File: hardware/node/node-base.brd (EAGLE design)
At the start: 100 x 80 mm, 19 parts, among them U1 INA322_DGK_8, U2 LMV551_DBV_5

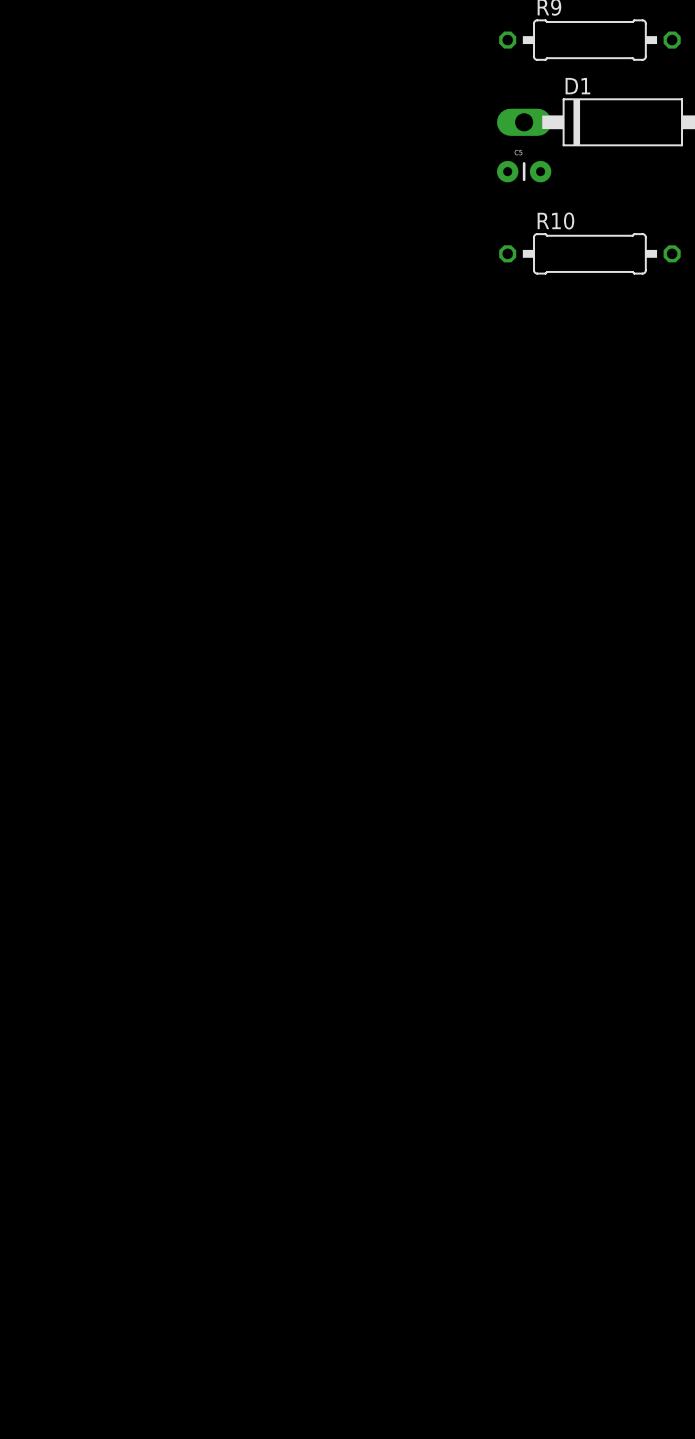
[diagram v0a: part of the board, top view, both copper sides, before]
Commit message: NODEHW: Added MCU power
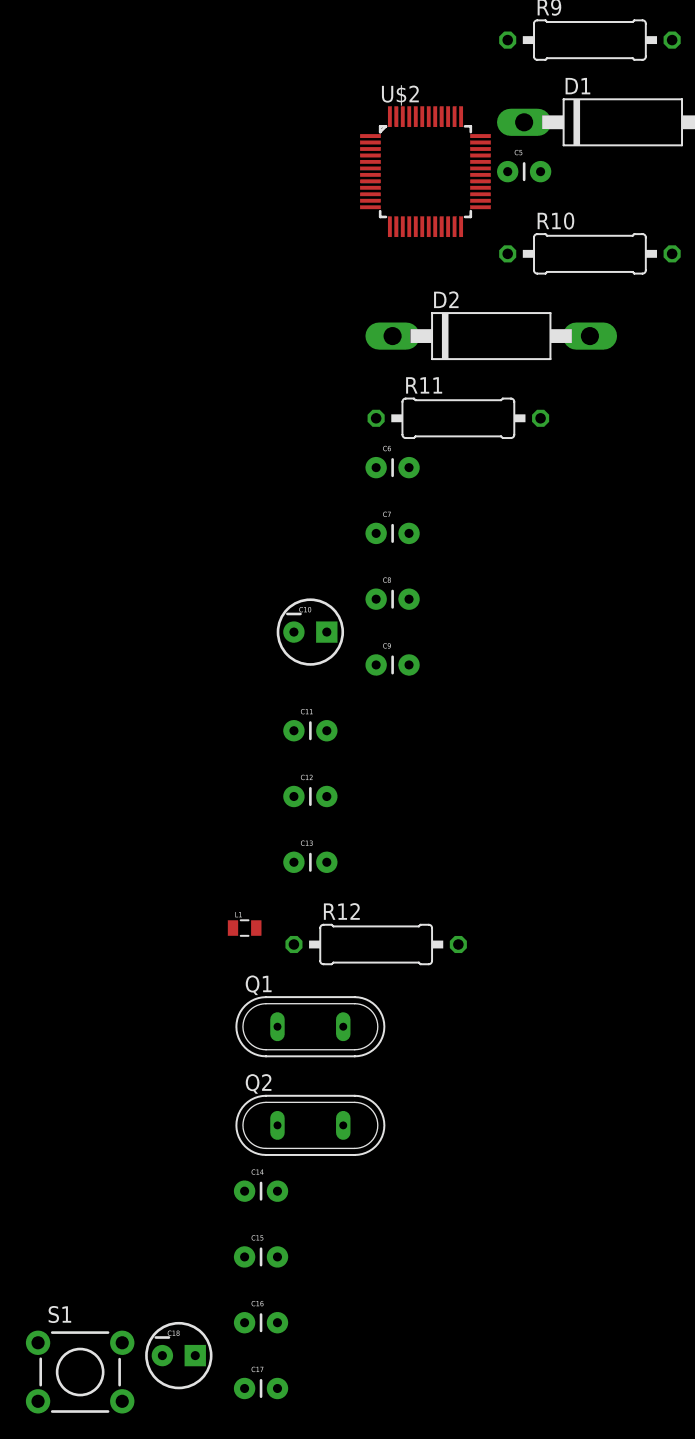
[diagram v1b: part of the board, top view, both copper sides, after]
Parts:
- added C10, C18: 10u, SparkFun-Capacitors:CPOL-RADIAL-10UF-25V
- added C11, C12, C13: 10n, SparkFun-Capacitors:CAP-PTH-SMALL
- added C14, C15, C16, C17: 7p5, SparkFun-Capacitors:CAP-PTH-SMALL
- added C6, C7, C8, C9: 100n, SparkFun-Capacitors:CAP-PTH-SMALL
- added D2: BAS81, diode:CB417-15
- added L1: (no value), SparkFun-Passives:0805
- added Q1, Q2: (no value), special:QS
- added R11: 10M, resistor:0309/12
- added R12: 1R, resistor:0309/12
- added S1: SPSTPTH_EZ, SparkFun-Electromechanical:TACTILE-PTH-EZ
- added U$2: EFM32ZG222EFM32ZG222F32, FullyCustom:QFP48
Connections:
- new net N$12: S1.3, U$2.16
- new net N$14: C14.1, Q1.1, U$2.12
- new net N$16: C15.1, Q1.2, U$2.11
- new net N$17: C16.1, Q2.1, U$2.21
- new net N$18: C17.1, Q2.2, U$2.20
- new net N$23: C18.1, U$2.29
- new net N$3: D2.A, R11.1, U$2.7
- new net N$6: L1.2, R12.1
- new net N$8: C11.1, C12.1, C13.1, R12.2, U$2.19, U$2.23
- net +3V3: now also C10.1, C6.1, C7.1, C8.1, C9.1, L1.1, U$2.22, U$2.28, U$2.4, U$2.43
- net DETECT_OUT: now also U$2.6
- net GND: now also C10.2, C11.2, C12.2, C13.2, C14.2, C15.2, C16.2, C17.2, C18.2, C6.2, C7.2, C8.2, C9.2, S1.1, U$2.18, U$2.44, U$2.5
- net N$2: now also R11.2
- net VCC/2: now also D2.C

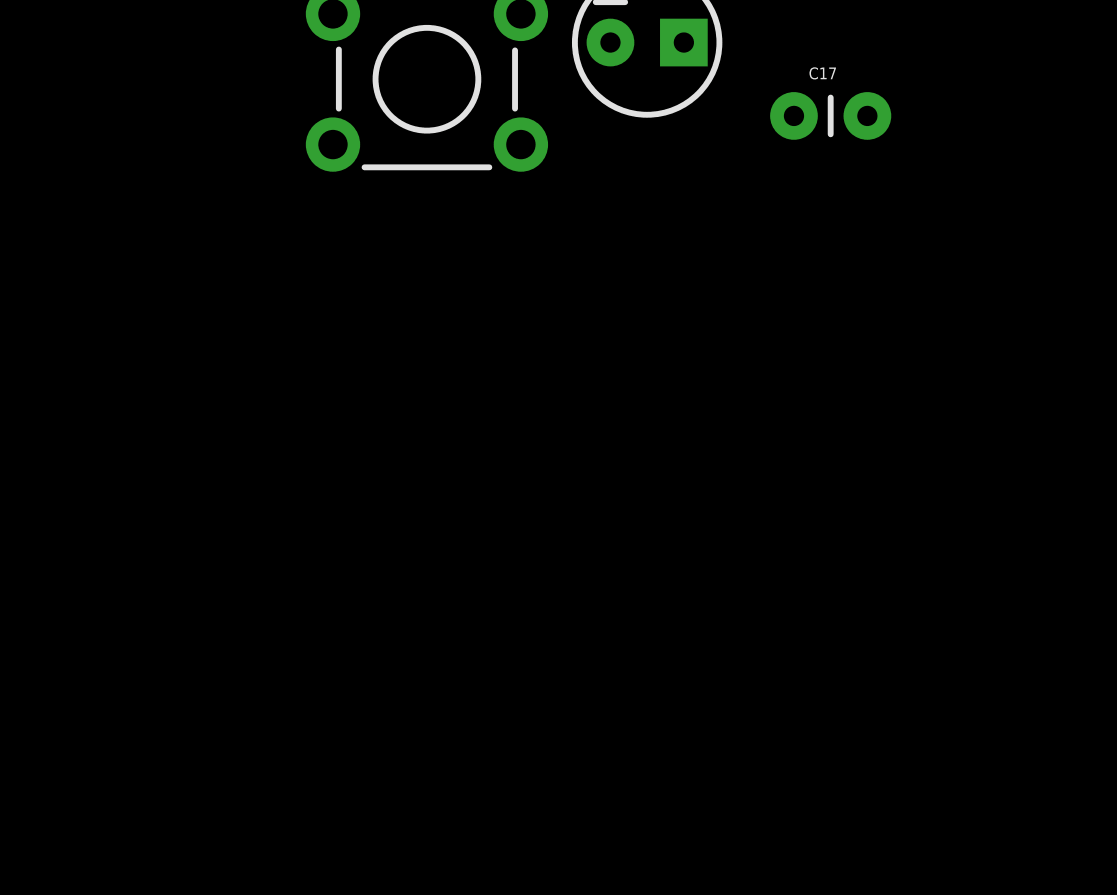
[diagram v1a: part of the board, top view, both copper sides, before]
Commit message: NODE: Added radio
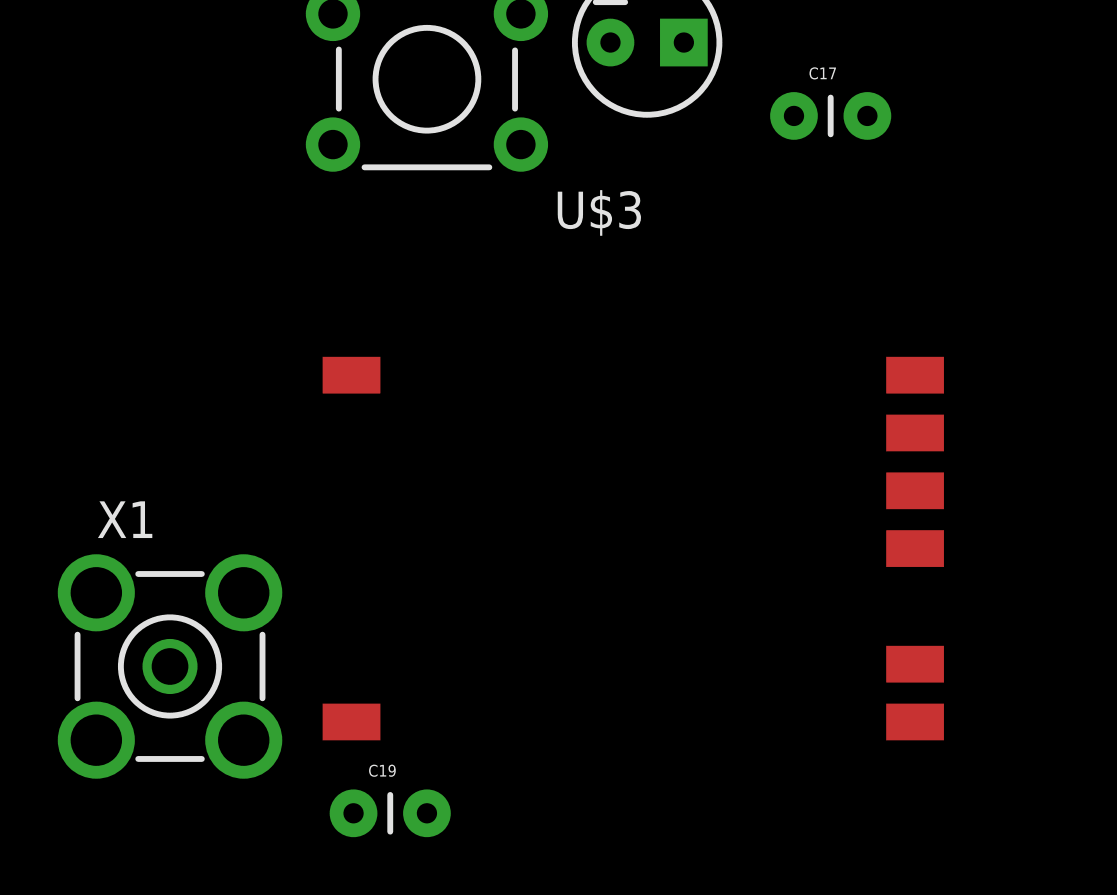
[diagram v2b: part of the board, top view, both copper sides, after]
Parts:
- added C19: 100n, SparkFun-Capacitors:CAP-PTH-SMALL
- added U$3: RFM69, Moteino:RFM69W-MINPADS
- added X1: BU-SMA-V, con-coax:BU-SMA-V
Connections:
- new net N$13: U$2.26, U$3.MISO
- new net N$15: U$2.27, U$3.MOSI
- new net N$19: U$2.35, U$3.NSS
- new net N$20: U$2.36, U$3.SCK
- new net N$22: U$3.ANA, X1.1
- net +3V3: now also C19.1, U$3.VDD
- net GND: now also C19.2, U$3.GND, X1.2, X1.3, X1.4, X1.5
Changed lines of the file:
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@@
 <element name="C18" library="SparkFun-Capacitors" package="CPOL-RADIAL-10UF-25V" value="10u" x="-67.31" y="-124.46"/>
 <element name="S1" library="SparkFun-Electromechanical" package="TACTILE-PTH-EZ" value="SPSTPTH_EZ" x="-74.93" y="-125.73"/>
+<element name="U$3" library="Moteino" package="RFM69W-MINPADS" value="RFM69" x="-66.04" y="-140.97"/>
+<element name="C19" library="SparkFun-Capacitors" package="CAP-PTH-SMALL" value="100n" x="-77.47" y="-151.13"/>
+<element name="X1" library="con-coax" package="BU-SMA-V" value="BU-SMA-V" x="-83.82" y="-146.05">
+<attribute name="OC_NEWARK" value="unknown" x="-83.82" y="-146.05" size="1.778" layer="27" display="off"/>
+<attribute name="MPN" value="" x="-83.82" y="-146.05" size="1.778" layer="27" display="off"/>
+<attribute name="MF" value="" x="-83.82" y="-146.05" size="1.778" layer="27" display="off"/>
+<attribute name="OC_FARNELL" value="unknown" x="-83.82" y="-146.05" size="1.778" layer="27" display="off"/>
+</element>
 </elements>
 <signals>
@@
 <contactref element="C18" pad="2"/>
 <contactref element="S1" pad="1"/>
+<contactref element="U$3" pad="GND"/>
+<contactref element="C19" pad="2"/>
+<contactref element="X1" pad="2"/>
+<contactref element="X1" pad="4"/>
+<contactref element="X1" pad="5"/>
+<contactref element="X1" pad="3"/>
+<wire x1="-86.3699" y1="-143.5001" x2="-86.3699" y2="-148.5999" width="0" layer="19" extent="1-1"/>
+<wire x1="-81.2701" y1="-148.5999" x2="-86.3699" y2="-148.5999" width="0" layer="19" extent="1-1"/>
+<wire x1="-81.2701" y1="-143.5001" x2="-86.3699" y2="-143.5001" width="0" layer="19" extent="1-1"/>
+<wire x1="-74.93" y1="-151.13" x2="-81.2701" y2="-148.5999" width="0" layer="19" extent="1-1"/>
+<wire x1="-58.04" y1="-147.97" x2="-74.93" y2="-151.13" width="0" layer="19" extent="1-1"/>
+<wire x1="-78.1812" y1="-123.4694" x2="-81.2701" y2="-143.5001" width="0" layer="19" extent="1-1"/>
 <wire x1="-68.58" y1="-124.46" x2="-78.1812" y2="-123.4694" width="0" layer="19" extent="1-1"/>
 <wire x1="-59.69" y1="-127" x2="-68.58" y2="-124.46" width="0" layer="19" extent="1-1"/>
@@
 <contactref element="C9" pad="1"/>
 <contactref element="L1" pad="1"/>
+<contactref element="U$3" pad="VDD"/>
+<contactref element="C19" pad="1"/>
+<wire x1="-77.54" y1="-147.97" x2="-77.47" y2="-151.13" width="0" layer="19" extent="1-1"/>
+<wire x1="-63.13" y1="-91.44" x2="-77.54" y2="-147.97" width="0" layer="19" extent="1-1"/>
 <wire x1="-52.07" y1="-71.12" x2="-63.13" y2="-91.44" width="0" layer="19" extent="1-1"/>
 <wire x1="-55.88" y1="-68.58" x2="-52.07" y2="-71.12" width="0" layer="19" extent="1-1"/>
@@
 <wire x1="-49.51" y1="-37.27" x2="-78.1812" y2="-127.9906" width="0" layer="19" extent="1-1"/>
 </signal>
+<signal name="N$13">
+<contactref element="U$2" pad="26"/>
+<contactref element="U$3" pad="MISO"/>
+<wire x1="-44.01" y1="-35.27" x2="-58.04" y2="-139.97" width="0" layer="19" extent="1-1"/>
+</signal>
+<signal name="N$15">
+<contactref element="U$3" pad="MOSI"/>
+<contactref element="U$2" pad="27"/>
+<wire x1="-44.01" y1="-34.77" x2="-58.04" y2="-137.97" width="0" layer="19" extent="1-1"/>
+</signal>
+<signal name="N$19">
+<contactref element="U$2" pad="35"/>
+<contactref element="U$3" pad="NSS"/>
+<wire x1="-44.01" y1="-30.77" x2="-58.04" y2="-135.97" width="0" layer="19" extent="1-1"/>
+</signal>
+<signal name="N$20">
+<contactref element="U$2" pad="36"/>
+<contactref element="U$3" pad="SCK"/>
+<wire x1="-44.01" y1="-30.27" x2="-58.04" y2="-141.97" width="0" layer="19" extent="1-1"/>
+</signal>
+<signal name="N$22">
+<contactref element="X1" pad="1"/>
+<contactref element="U$3" pad="ANA"/>
+<wire x1="-58.04" y1="-145.97" x2="-83.82" y2="-146.05" width="0" layer="19" extent="1-1"/>
+</signal>
 </signals>

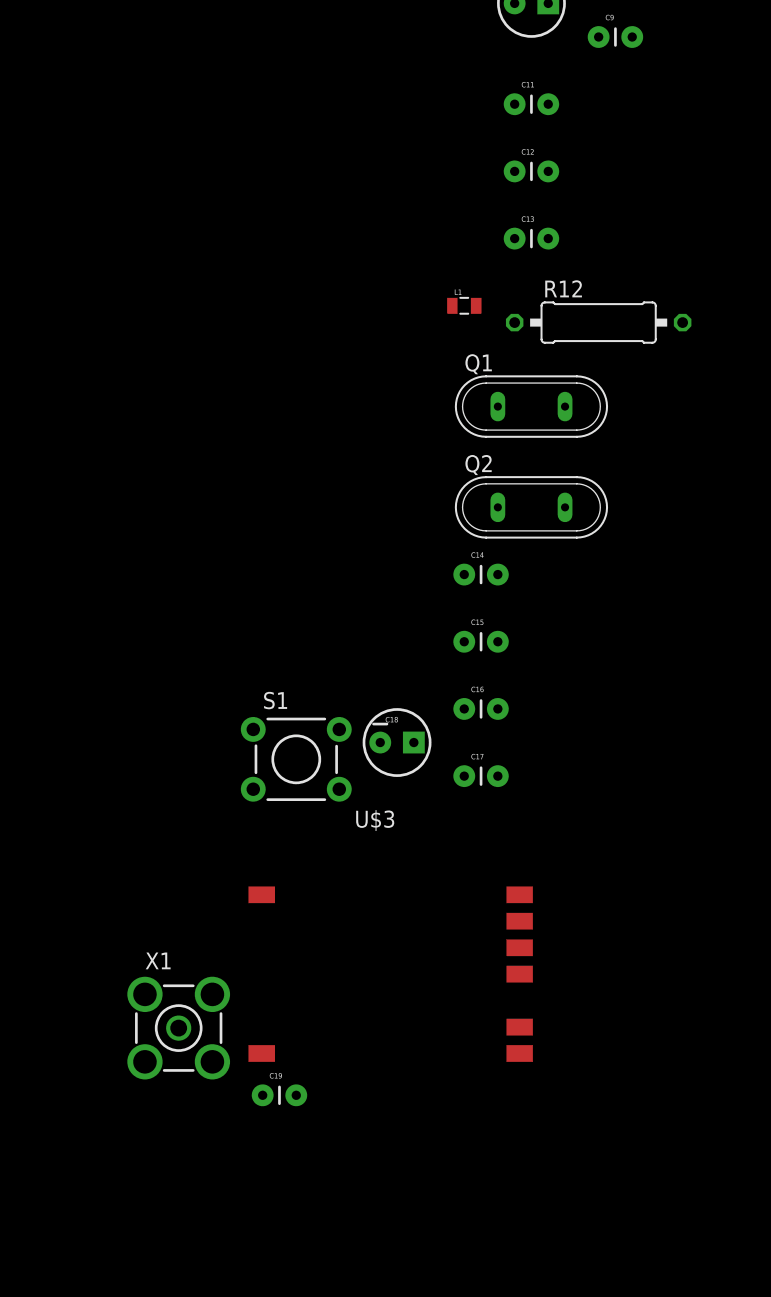
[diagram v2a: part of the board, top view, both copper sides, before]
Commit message: NODE: Added sensors, power control
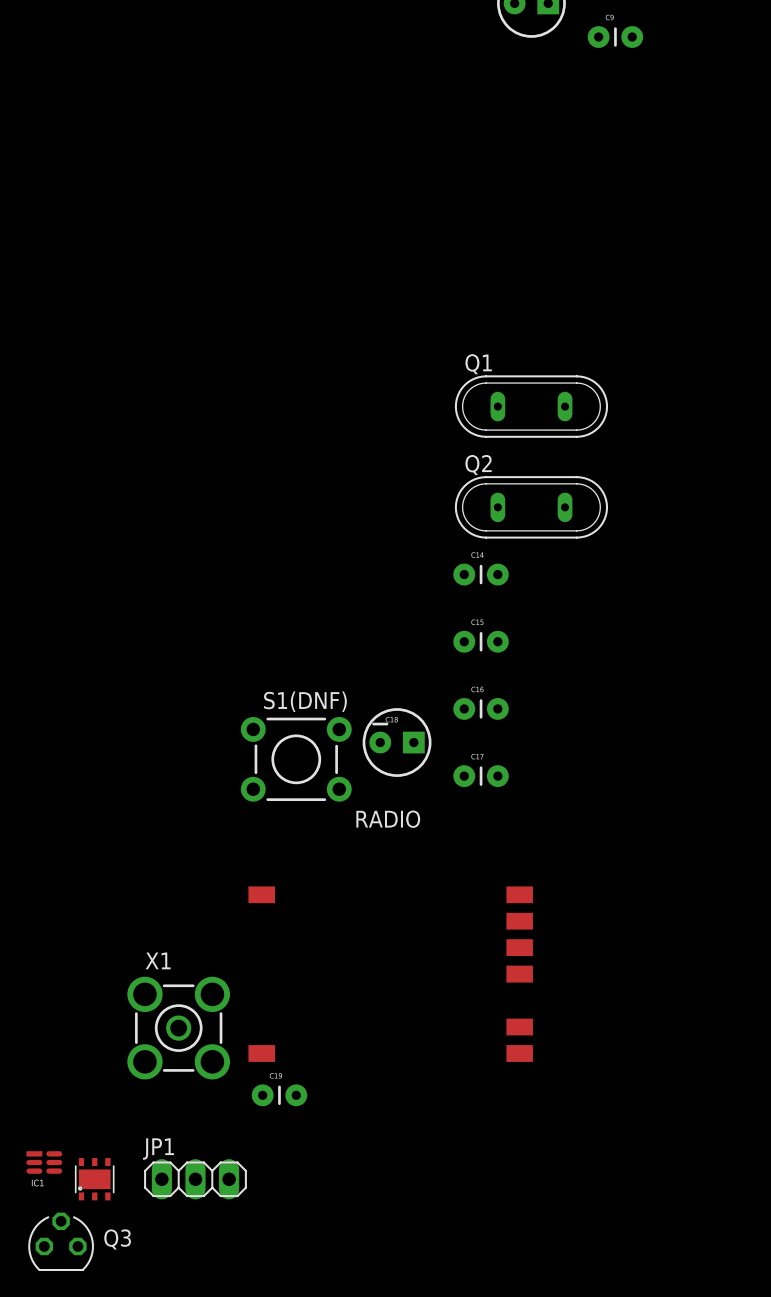
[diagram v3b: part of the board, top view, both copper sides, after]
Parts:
- removed C11, C12, C13: 10n, SparkFun-Capacitors:CAP-PTH-SMALL
- removed L1: (no value), SparkFun-Passives:0805
- removed R12: 1R, resistor:0309/12
- added IC1: HYPERTRIANGLE_TCS3472FN, lightsensor:HYPERTRIANGLE_DFN-6
- added JP1: (no value), pinhead:1X03
- added Q3: BS250, transistor-small-signal:SOT54E
- added RADIO: RFM69, Moteino:RFM69W-MINPADS
- U$3: value RFM69 -> SHT21; device Moteino:RFM69W-MINPADS -> SHT21:SHT21
- moved U$3 29.2 mm to (-90.2, -157.5)
- renumbered S1 to S1(DNF)
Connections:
- removed net N$6: L1.2, R12.1
- removed net N$8: C11.1, C12.1, C13.1, R12.2, U$2.19, U$2.23
- new net CON_EXTSENSOR: JP1.1, U$2.24
- new net N$21: RADIO.DIO0, U$2.17
- new net N$24: IC1.2, Q3.D, U$3.5
- new net N$25: IC1.1, U$2.48, U$3.6
- new net N$26: JP1.2, U$2.25
- new net N$27: IC1.6, U$2.47, U$3.1
- new net N$28: Q3.G, U$2.46
- net +3V3: now also Q3.S, RADIO.VDD, U$2.19, U$2.23; no longer L1.1, U$3.VDD
- net GND: now also IC1.3, JP1.3, RADIO.GND, U$3.2, U$3.P$1; no longer C11.2, C12.2, C13.2, U$3.GND
- net N$13: now also RADIO.MISO; no longer U$3.MISO
- net N$15: now also RADIO.MOSI; no longer U$3.MOSI
- net N$19: now also RADIO.NSS; no longer U$3.NSS
- net N$20: now also RADIO.SCK; no longer U$3.SCK
- net N$22: now also RADIO.ANA; no longer U$3.ANA

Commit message: NODEHW: Finished first schematic draft
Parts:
- added C11: 10n, SparkFun-Capacitors:CAP-PTH-SMALL
- added CON_EXTSENSOR: (no value), pinhead:1X03
- added LED1: RED, led:LED3MM
- added LED2: YELLOW, led:LED3MM
- added LED3: GREEN, led:LED3MM
- added R12: 1M, resistor:0309/12
- added R13, R14, R15: 220, resistor:0309/12
- added S1(DNF)1: SPSTPTH_EZ, SparkFun-Electromechanical:TACTILE-PTH-EZ
- JP1: device pinhead:1X03 -> pinhead:1X06
- Q1: value (none) -> 32.768kHz
- Q2: value (none) -> 24MHz
- U$2: value EFM32ZG222EFM32ZG222F32 -> EFM32ZG222F32
- moved JP1 12.0 mm to (-86.4, -168.9)
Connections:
- net N$1 renamed RGLINE
- net N$10 renamed INSTR_FILTERED
- net N$11 renamed OPAMP_VGND
- net N$13 renamed RADIO_MISO
- net N$14 renamed LFXTAL_P
- net N$15 renamed RADIO_MOSI
- net N$16 renamed LFXTAL_N
- net N$17 renamed XTALP
- net N$18 renamed XTALN
- net N$19 renamed RADIO_CS
- net N$2 renamed OPAMP_OUT
- net N$20 renamed RADIO_SCK
- net N$21 renamed RADIO_INT
- net N$22 renamed RADIO_ANT
- net N$23 renamed DECOUPLE
- net N$24 renamed EXT_PWRLINE
- net N$25 renamed SCL
- net N$27 renamed SDA
- net N$28 renamed EXT_PWRUP
- net N$3 renamed DETECT_REF
- net N$4 renamed PIEZO_FILTERED
- net N$5 renamed PIEZO_OUT
- net N$7 renamed REFLINE
- net N$9 renamed INSTR_OUT
- removed net CON_EXTSENSOR: JP1.1, U$2.24
- removed net N$12: S1(DNF).3, U$2.16
- removed net N$26: JP1.2, U$2.25
- new net EXTSENS_RX: CON_EXTSENSOR.2, U$2.25
- new net EXTSENS_TX: CON_EXTSENSOR.1, U$2.24
- new net LED_GREEN: LED3.A, U$2.40
- new net LED_RED: LED1.A, U$2.42
- new net LED_SWITCH: C11.1, R12.1, S1(DNF)1.3, U$2.45
- new net LED_YELLOW: LED2.A, U$2.41
- new net N$10: LED2.K, R14.2
- new net N$11: LED3.K, R15.2
- new net N$9: LED1.K, R13.2
- new net RESET: JP1.5, S1(DNF).3, U$2.16
- new net SWCLK: JP1.2, U$2.37
- new net SWDIO: JP1.4, U$2.38
- new net SWO: JP1.6, U$2.39
- net +3V3: now also JP1.1, R12.2
- net GND: now also C11.2, CON_EXTSENSOR.3, R13.1, R14.1, R15.1, S1(DNF)1.1

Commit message: NODEHW: Schematic basically finished
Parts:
- added C12, C13: 10n, SparkFun-Capacitors:CAP-PTH-SMALL
- added L1: (no value), resistor:0207/10
- added U$4: TPS61291DRV, FullyCustom:DRV0006A
- R1, R10, R11, R12, R13, R14, R15, R2, R3, R4, R5, R8, R9: device resistor:0309/12 -> resistor:0204/7
- moved U$2 123.0 mm to (52.1, 38.1)
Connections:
- new net N$4: L1.2, U$4.1
- new net V+: C12.1, L1.1, U$4.3, U$4.4
- net +3V3: now also C13.1, U$4.2
- net EXT_PWRUP: now also U$2.30
- net GND: now also C12.2, C13.2, U$4.5, U$4.6, U$4.7

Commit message: NODEHW: Some components placed...
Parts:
- added SW1: (no value), SparkFun-Electromechanical:DIPSWITCH-08
- D1, D2: device diode:CB417-15 -> diode:DO35-7
- R6, R7: device resistor:0309/12 -> resistor:0204/7
- moved R15 367.7 mm to (141.0, 67.3)
- moved R14 360.8 mm to (142.2, 63.5)
- moved R13 353.2 mm to (124.5, 74.9)
- moved LED1 341.2 mm to (130.8, 83.8)
- moved LED2 341.2 mm to (130.8, 78.7)
- moved LED3 341.2 mm to (130.8, 73.7)
- moved C11 331.1 mm to (78.7, 82.5)
- moved R12 322.6 mm to (81.3, 78.7)
- moved JP1 276.2 mm to (54.6, 68.6), turned to 180 degrees
- moved S1(DNF) 264.4 mm to (81.3, 87.6)
- moved C13 258.7 mm to (2.54, 5.08), turned to 90 degrees
- moved C12 257.3 mm to (10.2, 5.08), turned to 90 degrees
- moved U$4 248.8 mm to (6.35, 6.35), turned to 90 degrees
- moved L1 247.7 mm to (6.35, 2.54), turned to 180 degrees
- moved C19 238.7 mm to (73.6, 33.8), turned to 270 degrees
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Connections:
- new net SW_ADDR_1: SW1.16, U$2.15
- new net SW_ADDR_2: SW1.15, U$2.14
- new net SW_ADDR_3: SW1.14, U$2.13
- new net SW_ADDR_4: SW1.13, U$2.3
- new net SW_ADDR_5: SW1.12, U$2.2
- new net SW_ADDR_6: SW1.11, U$2.1
- new net SW_ADDR_7: SW1.10, U$2.33
- new net SW_ADDR_8: SW1.9, U$2.34
- net +3V3: now also R11.2
- net GND: now also SW1.1, SW1.2, SW1.3, SW1.4, SW1.5, SW1.6, SW1.7, SW1.8
- net OPAMP_OUT: no longer R11.2
